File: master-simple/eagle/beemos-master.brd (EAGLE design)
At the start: 99.1 x 73.7 mm, 56 parts, among them CON1 BATTERY, CON2 JACK_DC_BARREL, CON3 SPI, IC1 32U4, IC2 MCP73831T, IC3 MCP1703CB, IC4 DMP1045U, J1 RJ12STRAIGHT-I2C, J2 RJ12STRAIGHT-I2C, J3 RJ12STRAIGHT-I2C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

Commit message: master: cleanup
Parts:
- moved R15 8.98 mm to (11.4, 57.8), turned to 0 degrees
- moved D2 8.82 mm to (11.4, 53.3)
- moved C11 6.48 mm to (47.0, 52.7), turned to 270 degrees
- moved R18 1.80 mm to (41.9, 52.7), turned to 90 degrees
- moved R19 1.42 mm to (44.5, 52.7), turned to 270 degrees
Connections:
- net N$7: now also IC2.1
- net SCL: no longer R1.1
- net SDA: now also R1.1
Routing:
- net N$5: track 83.0 -> 60.4 mm
- net VBAT1: track 142.0 -> 126.7 mm, vias 2 -> 3
- net VDD: track 150.0 -> 135.7 mm, vias 3 -> 0
- net SDA: track 89.3 -> 103.4 mm
- net GND: track 119.5 -> 108.7 mm, vias 25 -> 24
- net 3.3V: track 221.1 -> 213.8 mm
- net ISP+5V: track 123.0 -> 115.9 mm
- net A6: track 28.3 -> 25.7 mm

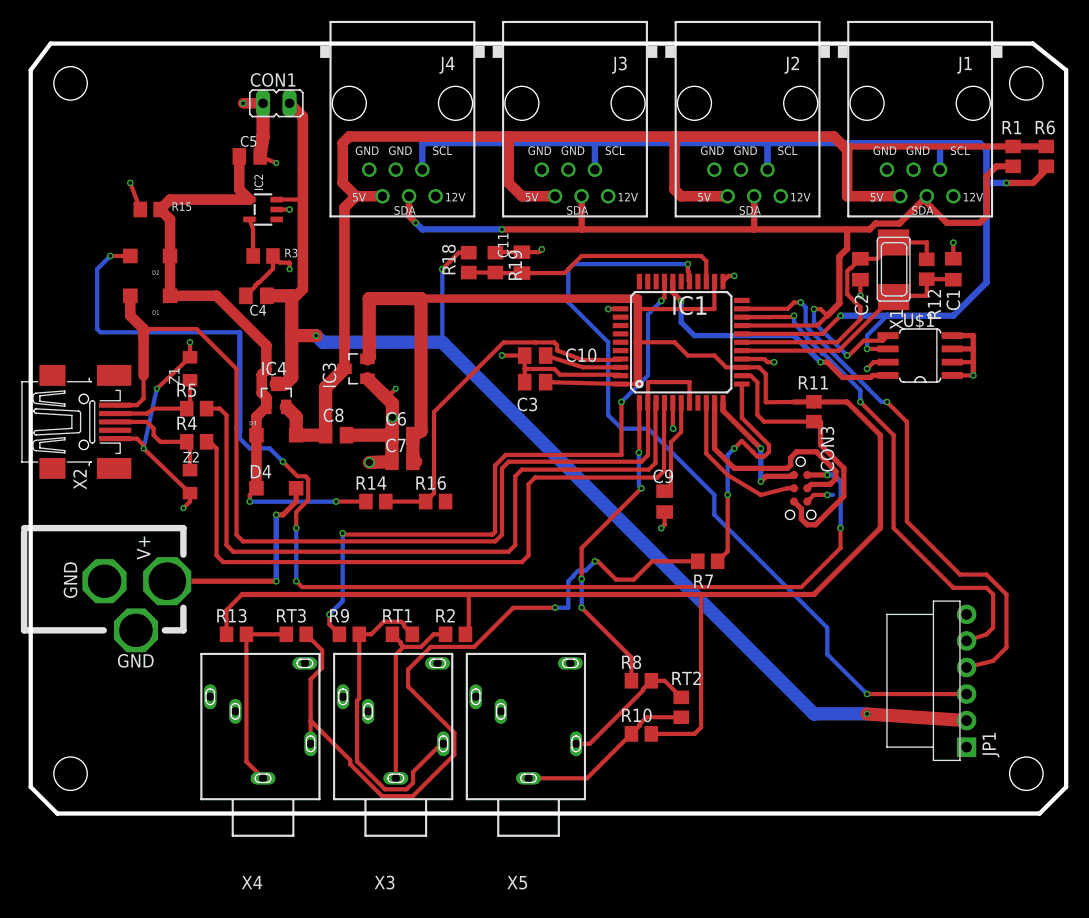
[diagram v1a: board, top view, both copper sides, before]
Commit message: Arranged labels and resistors in beemos master board layout
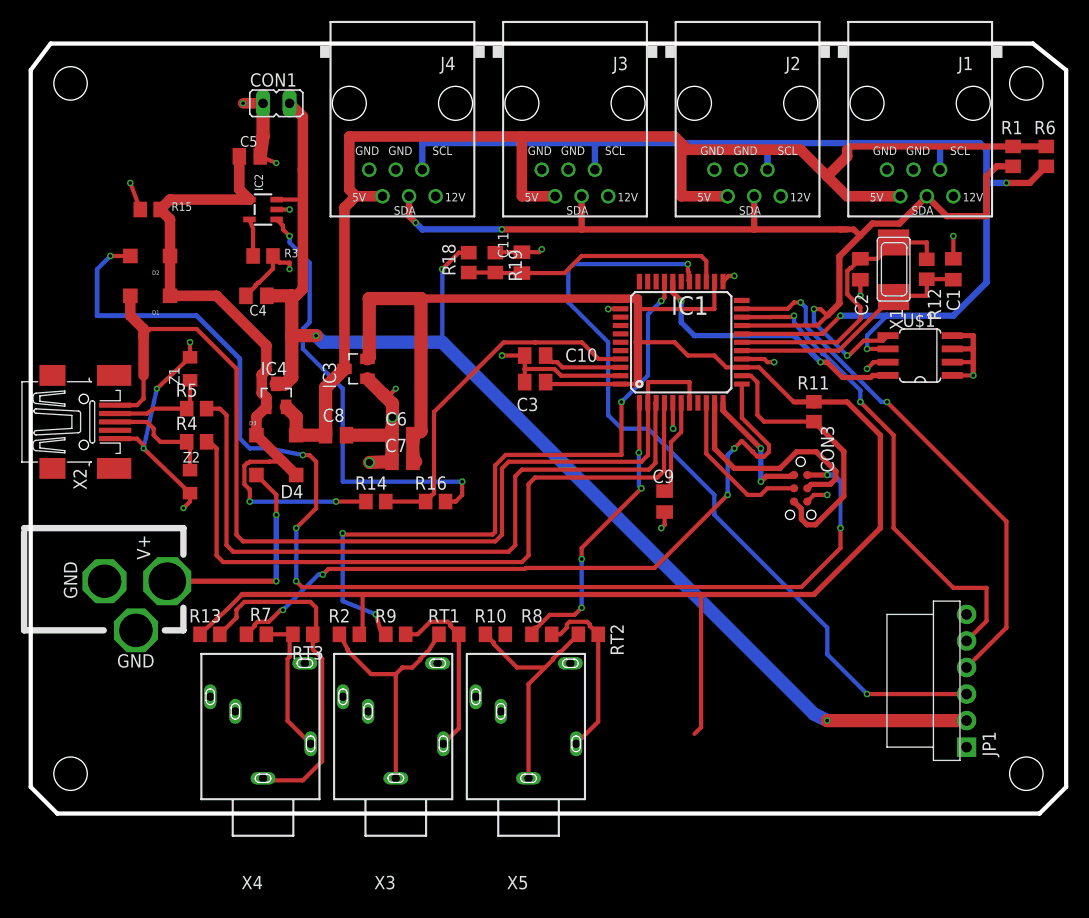
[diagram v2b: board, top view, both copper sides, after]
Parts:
- D4: value ||Schottky -> Schottky||
- moved R7 43.7 mm to (21.6, 17.1), turned to 0 degrees
- moved R10 16.9 mm to (44.5, 17.1)
- moved RT2 11.3 mm to (53.3, 17.1), turned to 0 degrees
- moved R8 10.5 mm to (48.9, 17.1)
- moved R2 10.2 mm to (30.5, 17.1)
- moved RT1 4.45 mm to (40.0, 17.1)
- moved R9 4.44 mm to (34.9, 17.1)
- moved R13 2.54 mm to (17.1, 17.1)
- moved D4 1.27 mm to (23.5, 32.4), turned to 180 degrees
- moved RT3 0.64 mm to (26.0, 17.1), turned to 180 degrees
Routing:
- net N$2: track 75.1 -> 14.0 mm, vias 2 -> 0
- net D11: track 23.4 -> 68.3 mm, vias 2 -> 4
- net N$7: track 0.00 -> 42.8 mm, vias 0 -> 2
- net N$4: track 18.2 -> 33.8 mm
- net N$21: track 30.2 -> 17.2 mm
- net N$5: track 60.4 -> 66.6 mm
- net N$9: track 17.1 -> 22.9 mm
- net N$14: track 19.0 -> 23.3 mm
- net 3.3V: track 213.8 -> 209.9 mm
- net N$8: track 13.3 -> 17.1 mm
- net D7: track 31.0 -> 28.1 mm
- net TX: track 53.3 -> 50.8 mm
- net D10: track 62.5 -> 64.6 mm
- net VDD: track 135.7 -> 134.5 mm
- net RX: track 47.5 -> 46.4 mm
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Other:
- board text added: "I2C_1"
- board text added: "I2C_2"
- board text added: "I2C_3"
- board text added: "I2C_4"

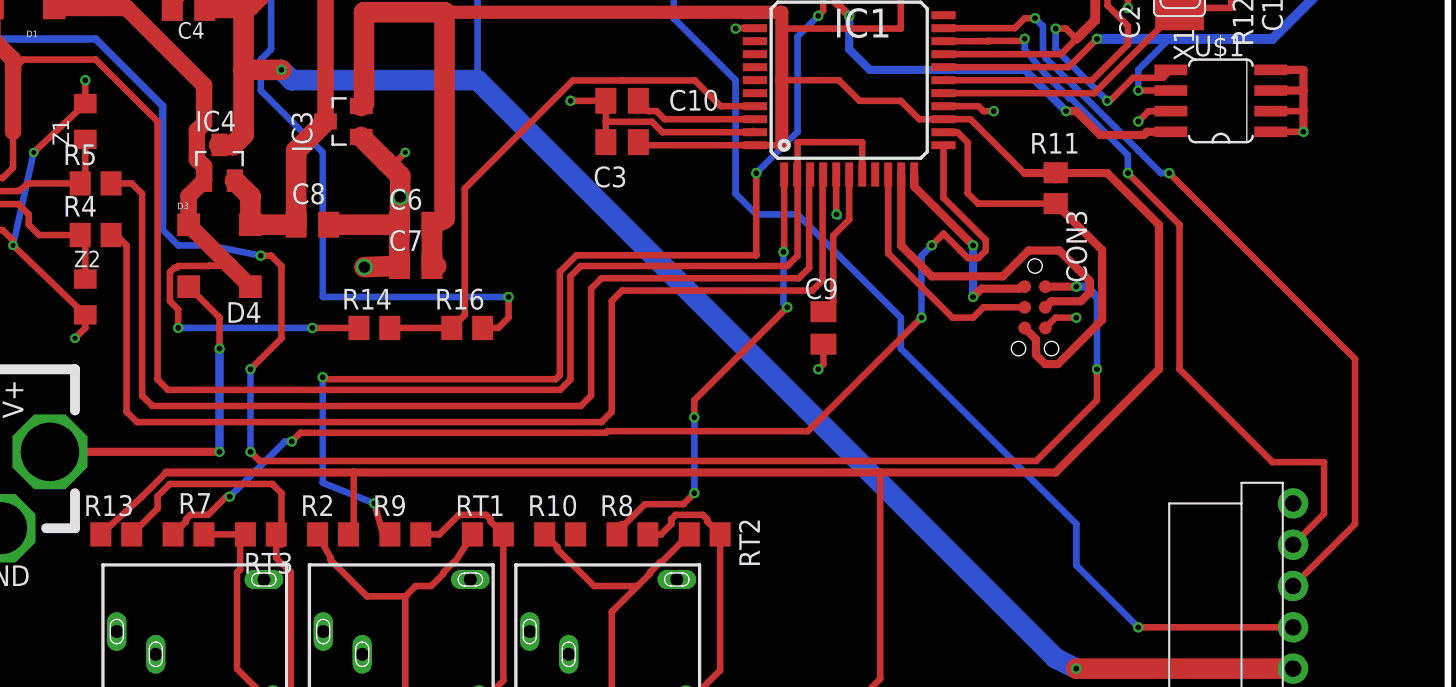
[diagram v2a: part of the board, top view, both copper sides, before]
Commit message: Fixed airwires/clearance for beemos master board
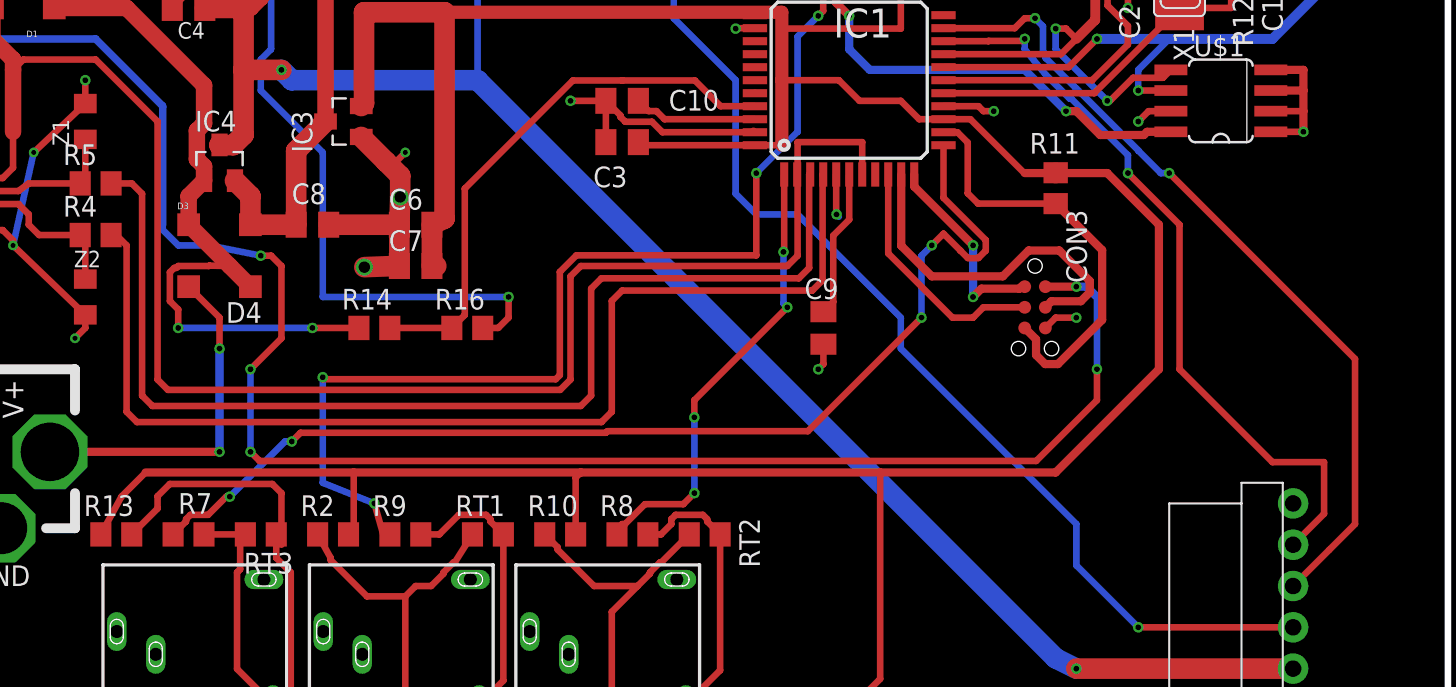
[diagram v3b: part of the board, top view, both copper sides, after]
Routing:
- net 3.3V: track 209.9 -> 214.3 mm
- net GND: track 108.9 -> 109.5 mm
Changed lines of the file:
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@@
 <wire x1="21.955" y1="62.865" x2="23.495" y2="62.23" width="0.4064" layer="1"/>
 <via x="23.495" y="62.23" extent="1-16" drill="0.3048"/>
-<wire x1="47.26" y1="43.815" x2="47.26" y2="42.545" width="0.4064" layer="1"/>
 <wire x1="56.43" y1="41.885" x2="56.338940625" y2="41.976059375" width="0.4064" layer="1"/>
 <contactref element="J1" pad="GND2"/>
@@
 <wire x1="48.625" y1="53.705" x2="48.895" y2="53.975" width="0.4064" layer="1"/>
 <via x="48.895" y="53.975" extent="1-16" drill="0.35"/>
-<wire x1="47.26" y1="42.5282" x2="47.26" y2="41.275" width="0.4064" layer="1"/>
-<wire x1="47.26" y1="42.5282" x2="50.09771875" y2="42.5282" width="0.4064" layer="1"/>
 <wire x1="50.74091875" y1="41.885" x2="56.43" y2="41.885" width="0.4064" layer="1"/>
 <wire x1="50.09771875" y1="42.5282" x2="50.74091875" y2="41.885" width="0.4064" layer="1"/>
-<wire x1="81.915" y1="61.595" x2="84.455" y2="61.595" width="0" layer="19" extent="1-1"/>
-<wire x1="88.265" y1="55.245" x2="84.455" y2="61.595" width="0" layer="19" extent="1-1"/>
-<wire x1="88.1634" y1="45.72" x2="88.265" y2="53.07" width="0" layer="19" extent="1-1"/>
-<wire x1="82.0166" y1="43.18" x2="88.1634" y2="43.18" width="0" layer="19" extent="1-1"/>
-<wire x1="79.375" y1="49.53" x2="80.645" y2="43.18" width="0" layer="19" extent="1-1"/>
-<wire x1="71.12" y1="43.18" x2="80.01" y2="42.545" width="0" layer="19" extent="1-1"/>
-<wire x1="66.23" y1="50.885" x2="68.03" y2="43.485" width="0" layer="19" extent="1-1"/>
-<wire x1="61.43" y1="39.285" x2="68.03" y2="43.485" width="0" layer="19" extent="1-1"/>
-<wire x1="56.43" y1="41.885" x2="61.43" y2="39.285" width="0" layer="19" extent="1-1"/>
-<wire x1="47.26" y1="42.545" x2="47.26" y2="42.5282" width="0" layer="19" extent="1-1"/>
-<wire x1="56.43" y1="48.285" x2="56.338940625" y2="41.976059375" width="0" layer="19" extent="1-1"/>
-<wire x1="60.6425" y1="28.845" x2="61.595" y2="36.6844" width="0" layer="19" extent="1-16"/>
-<wire x1="48.895" y1="53.975" x2="55.27" y2="48.285" width="0" layer="19" extent="1-1"/>
-<wire x1="48.895" y1="61.595" x2="48.895" y2="53.975" width="0" layer="19" extent="1-1"/>
-<wire x1="51.435" y1="61.595" x2="48.895" y2="61.595" width="0" layer="19" extent="1-1"/>
-<wire x1="67.945" y1="61.595" x2="67.31" y2="51.435" width="0" layer="19" extent="1-1"/>
-<wire x1="65.405" y1="61.595" x2="67.945" y2="61.595" width="0" layer="19" extent="1-1"/>
-<wire x1="34.925" y1="40.64" x2="45.085" y2="43.815" width="0" layer="19" extent="1-1"/>
-<wire x1="34.925" y1="61.595" x2="44.5" y2="53.705" width="0" layer="19" extent="1-1"/>
-<wire x1="32.385" y1="61.595" x2="34.925" y2="61.595" width="0" layer="19" extent="1-1"/>
-<wire x1="24.765" y1="57.785" x2="32.385" y2="61.595" width="0" layer="19" extent="1-1"/>
-<wire x1="23.495" y1="62.23" x2="23.5251" y2="57.785" width="0" layer="19" extent="1-1"/>
-<wire x1="23.175" y1="53.34" x2="23.5251" y2="57.785" width="0" layer="19" extent="1-1"/>
-<wire x1="15.24" y1="45.085" x2="20.59" y2="49.53" width="0" layer="19" extent="1-1"/>
-<wire x1="7.065" y1="22.225" x2="14.605" y2="29.21" width="0" layer="19" extent="1-1"/>
-<wire x1="10.48" y1="57.785" x2="21.955" y2="62.865" width="0" layer="19" extent="1-1"/>
-<wire x1="76.2" y1="30.48" x2="80.01" y2="42.545" width="0" layer="19" extent="1-1"/>
-<wire x1="17.175" y1="11.17" x2="7.065" y2="22.225" width="0" layer="19" extent="1-1"/>
-<wire x1="29.875" y1="11.17" x2="17.175" y2="11.17" width="0" layer="19" extent="1-1"/>
-<wire x1="42.575" y1="11.17" x2="29.875" y2="11.17" width="0" layer="19" extent="1-1"/>
-<wire x1="89.535" y1="19.05" x2="76.2" y2="30.48" width="0" layer="19" extent="1-1"/>
+<wire x1="47.26" y1="43.815" x2="47.26" y2="41.275" width="0.4064" layer="1"/>
+<wire x1="47.26" y1="43.815" x2="48.1568" y2="42.9182" width="0.4064" layer="1"/>
+<wire x1="48.1568" y1="42.9182" x2="48.1568" y2="42.82728125" width="0.4064" layer="1"/>
+<wire x1="48.1568" y1="42.82728125" x2="48.45588125" y2="42.5282" width="0.4064" layer="1"/>
+<wire x1="48.45588125" y1="42.5282" x2="50.09771875" y2="42.5282" width="0.4064" layer="1"/>
 </signal>
 <signal name="SCK">
@@
 <wire x1="80.0314" y1="40.74583125" x2="80.0314" y2="40.7327125" width="0.4064" layer="16"/>
 <wire x1="80.0314" y1="40.7327125" x2="81.3941125" y2="39.37" width="0.4064" layer="16"/>
-<wire x1="93.345" y1="17.78" x2="89.535" y2="13.97" width="0.4064" layer="1"/>
+<wire x1="93.345" y1="17.78" x2="91.7575" y2="16.1925" width="0.4064" layer="1"/>
+<wire x1="91.7575" y1="16.1925" x2="89.535" y2="13.97" width="0.4064" layer="1"/>
 <wire x1="81.915" y1="39.37" x2="93.345" y2="27.94" width="0.4064" layer="1"/>
 <wire x1="93.345" y1="27.94" x2="93.345" y2="17.78" width="0.4064" layer="1"/>
@@
 <wire x1="81.28" y1="36.195" x2="81.28" y2="27.305" width="0.508" layer="1"/>
 <wire x1="74.93" y1="20.955" x2="64.135" y2="20.955" width="0.508" layer="1"/>
-<wire x1="64.135" y1="20.955" x2="31.75" y2="20.955" width="0.508" layer="1"/>
-<wire x1="31.75" y1="20.955" x2="20.21676875" y2="20.955" width="0.508" layer="1"/>
+<wire x1="64.135" y1="20.955" x2="45.72" y2="20.955" width="0.508" layer="1"/>
+<wire x1="45.72" y1="20.955" x2="31.75" y2="20.955" width="0.508" layer="1"/>
+<wire x1="31.75" y1="20.955" x2="18.94676875" y2="20.955" width="0.508" layer="1"/>
 <wire x1="81.28" y1="27.305" x2="74.93" y2="20.955" width="0.508" layer="1"/>
 <contactref element="R2" pad="2"/>
@@
 <wire x1="63.5" y1="7.62" x2="64.135" y2="8.255" width="0.4064" layer="1"/>
 <wire x1="64.135" y1="8.255" x2="64.135" y2="20.955" width="0.4064" layer="1"/>
-<wire x1="16.195" y1="17.145" x2="18.735" y2="19.47323125" width="0.4064" layer="1"/>
-<wire x1="18.735" y1="19.47323125" x2="20.21676875" y2="20.955" width="0.4064" layer="1"/>
+<wire x1="16.195" y1="17.145" x2="17.465" y2="19.47323125" width="0.4064" layer="1"/>
+<wire x1="17.465" y1="19.47323125" x2="18.94676875" y2="20.955" width="0.4064" layer="1"/>
 <wire x1="72.997990625" y1="39.371909375" x2="73.024978125" y2="39.371909375" width="0.4064" layer="1"/>
 <wire x1="69.6849" y1="42.685" x2="72.997990625" y2="39.371909375" width="0.4064" layer="1"/>
@@
 <wire x1="31.43" y1="17.145" x2="31.75" y2="16.83" width="0.4064" layer="1"/>
 <wire x1="31.75" y1="16.83" x2="31.75" y2="20.955" width="0.4064" layer="1"/>
-<wire x1="31.75" y1="16.83" x2="45.4" y2="17.145" width="0" layer="19" extent="1-1"/>
+<wire x1="45.4" y1="17.145" x2="45.4" y2="20.635" width="0.4064" layer="1"/>
+<wire x1="45.4" y1="20.635" x2="45.72" y2="20.955" width="0.4064" layer="1"/>
 </signal>
 <signal name="N$21" class="1">

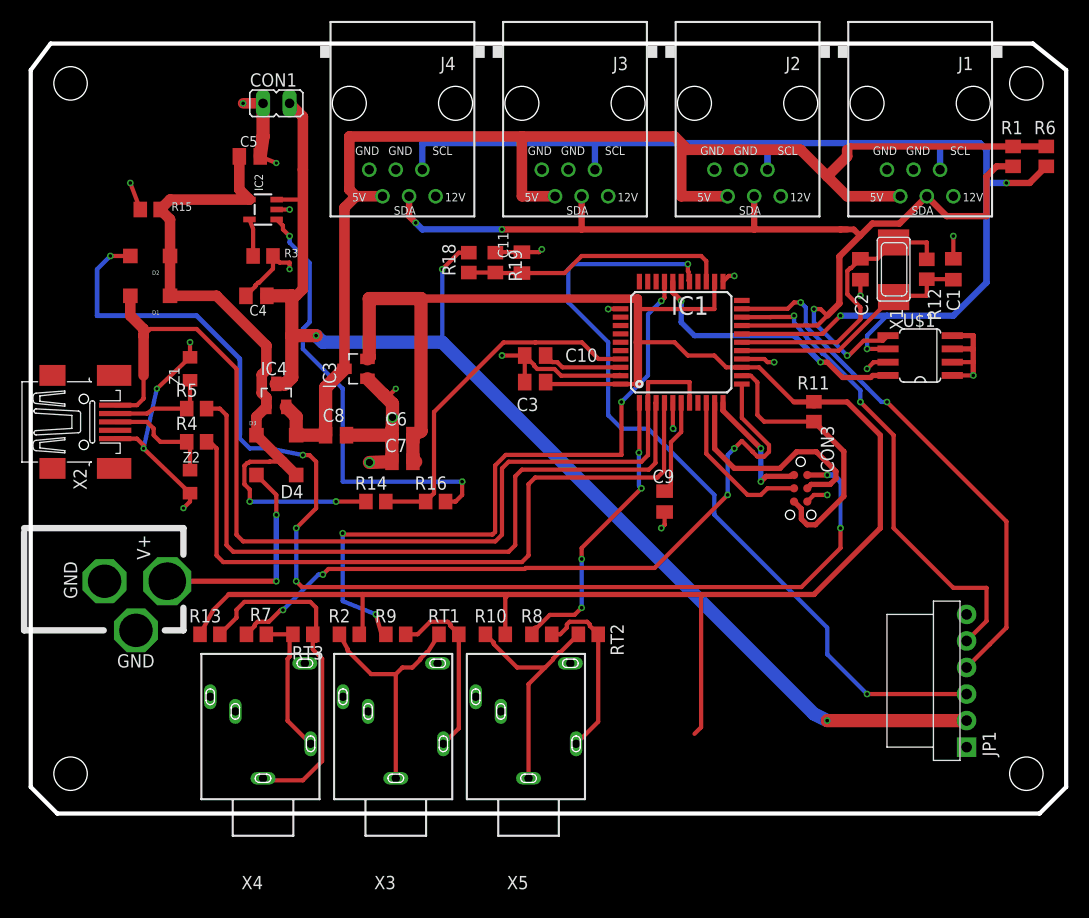
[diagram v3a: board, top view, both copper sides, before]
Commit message: Added power/com LEDs, extra pins exposed, cristal symmetric
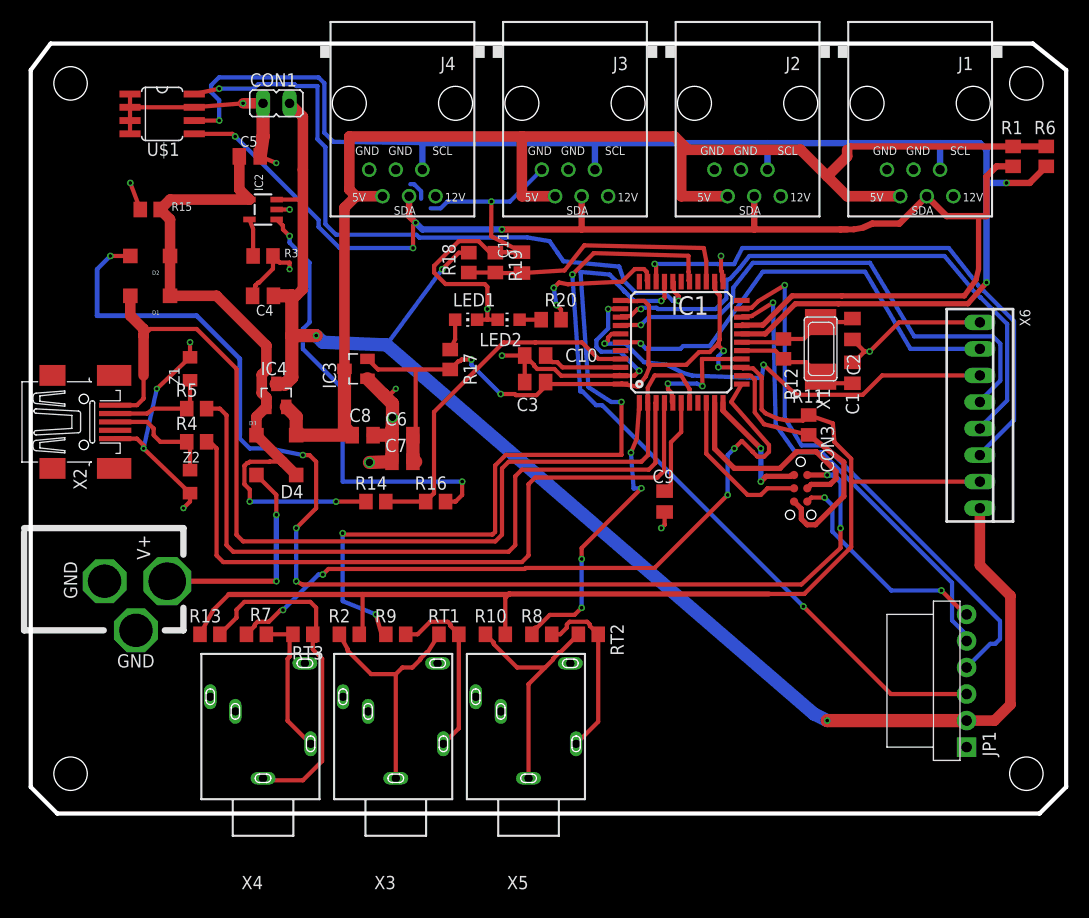
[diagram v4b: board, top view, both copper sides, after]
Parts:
- added LED1: red, led:CHIP-LED0805
- added LED2: white, led:CHIP-LED0805
- added R17, R20: 10k, rcl:R0805
- added X6: 22-23-2081, con-molex:22-23-2081
- C1, C2: value 18pF -> 22pF
- moved U$1 75.0 mm to (12.6, 65.0), turned to 270 degrees
- moved R12 15.7 mm to (72.0, 44.5)
- moved C1 13.8 mm to (78.6, 42.2)
- moved X1 10.3 mm to (75.6, 44.5)
- moved C2 5.77 mm to (78.6, 46.4)
- moved C8 2.54 mm to (31.8, 36.2)
- moved R11 1.37 mm to (74.4, 37.2)
- moved C4 0.64 mm to (22.2, 49.5)
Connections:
- new net N$10: LED1.A, R17.1
- new net N$11: LED2.A, R20.1
- net 3.3V: now also R17.2, X6.7
- net A0: now also X6.5
- net A1: now also X6.4
- net A2: now also X6.3
- net A3: now also X6.2
- net D13: now also R20.2
- net D5: now also X6.6
- net GND: now also LED1.C, LED2.C, X6.1
- net VBAT1: now also X6.8
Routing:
- net GND: track 109.5 -> 196.5 mm
- net A0: track 0.00 -> 54.6 mm, vias 0 -> 1
- net D5: track 0.01 -> 54.4 mm, vias 0 -> 1
- net A1: track 0.00 -> 50.4 mm, vias 0 -> 1
- net A3: track 0.00 -> 42.6 mm, vias 0 -> 1
- net A2: track 0.00 -> 41.9 mm, vias 0 -> 2
- net D9: track 26.3 -> 64.9 mm
- net 3.3V: track 214.3 -> 180.5 mm, vias 0 -> 4
- net SDA: track 103.5 -> 132.2 mm
- net SCL: track 114.9 -> 140.9 mm
- net VBAT1: track 126.8 -> 151.4 mm
- net N$42: track 27.7 -> 11.5 mm
- net D13: track 0.00 -> 14.0 mm, vias 0 -> 2
- net D10: track 64.6 -> 76.9 mm
- net XTAL1: track 24.1 -> 11.9 mm
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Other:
- board text added: "3.3V"
- board text added: "A0"
- board text added: "A1"
- board text added: "A2"
- board text added: "A3"
- board text added: "D5"
- board text added: "VBAT1"
